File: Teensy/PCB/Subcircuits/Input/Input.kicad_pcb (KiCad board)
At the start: 2 copper layers, 4 parts

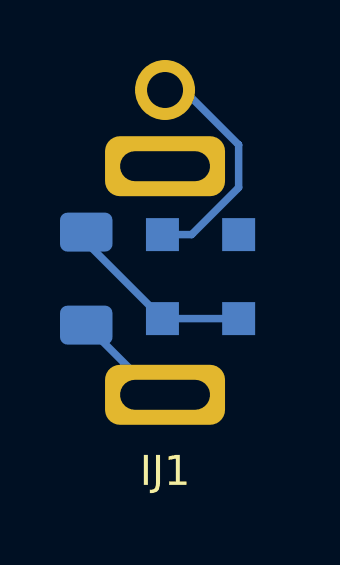
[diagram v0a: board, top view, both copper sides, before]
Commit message: Added Panel PCBs
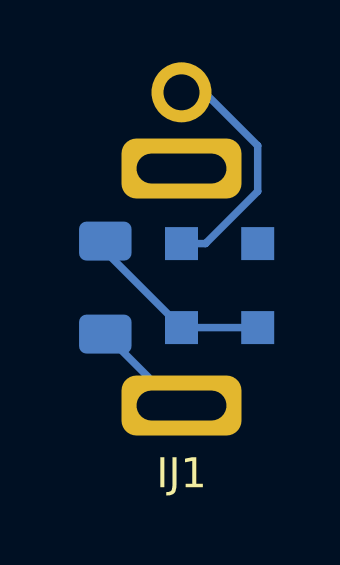
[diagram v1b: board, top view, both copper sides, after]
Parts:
- moved ID1 0.70 mm to (88.9, 90.3)
- moved IR1 0.70 mm to (86.4, 90.3)
- moved ID2 0.70 mm to (91.4, 90.3)
- moved IJ1 0.55 mm to (88.9, 88.9)
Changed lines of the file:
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@@
   (net 0 "")
   (footprint "Perfboard:3.5mm Jack Perfboard" (layer "F.Cu")
-    (at 88.351 88.822274)
-    (property "Sheetfile" "../Subcircuits/Input/Input.kicad_sch")
-    (property "Sheetname" "Attack_Time_Mod_In")
+    (at 88.9 88.9)
+    (property "Sheetfile" "Input.kicad_sch")
+    (property "Sheetname" "")
     (attr through_hole)
     (fp_text reference "IJ1" (at 0 7.62 unlocked) (layer "F.SilkS")
@@
       (effects (font (size 1 1) (thickness 0.15)))
     )
-    (fp_line (start 2.54 -3.81) (end 3.81 -3.81) (layer "Dwgs.User") (width 0.12))
-    (fp_line (start 2.54 -3.81) (end -2.54 -3.81) (layer "Dwgs.User") (width 0.12))
-    (fp_line (start -3.81 6.35) (end -2.54 6.35) (layer "Dwgs.User") (width 0.12))
-    (fp_line (start -2.54 6.35) (end 2.54 6.35) (layer "Dwgs.User") (width 0.12))
-    (fp_line (start 3.81 6.35) (end 2.54 6.35) (layer "Dwgs.User") (width 0.12))
-    (fp_line (start 3.81 -3.81) (end 3.81 6.35) (layer "Dwgs.User") (width 0.12))
-    (fp_line (start -3.81 -3.81) (end -3.81 6.35) (layer "Dwgs.User") (width 0.12))
-    (fp_line (start -2.54 -3.81) (end -3.81 -3.81) (layer "Dwgs.User") (width 0.12))
-    (fp_circle (center 0 0.83) (end 3.25 0.83) (layer "User.2") (width 0.12) (fill none))
+    (fp_rect (start -3.8 -3.94) (end 3.8 6.56) (layer "F.CrtYd") (width 0.12) (fill none))
+    (fp_circle (center 0 0.86) (end 3.25 0.86) (layer "User.2") (width 0.12) (fill none))
     (pad "G" thru_hole circle (at 0 -5.08) (size 2 2) (drill 1.2) (layers *.Cu *.Mask)
       (pintype "passive"))
     (pad "S" thru_hole roundrect (at 0 -2.54) (size 4 2) (drill oval 3 1) (layers *.Cu *.Mask) (roundrect_rratio 0.25)
       (pintype "passive"))
-    (pad "T" thru_hole roundrect (at 0 5.08) (size 4 2) (drill oval 3 1) (layers *.Cu *.Mask) (roundrect_rratio 0.25)
+    (pad "T" thru_hole roundrect (at 0 5.36) (size 4 2) (drill oval 3 1) (layers *.Cu *.Mask) (roundrect_rratio 0.25)
       (pintype "passive"))
     (model "C:/Users/Florian/Documents/KiCad/6.0/3dmodels/PTV09/PJ301M-12 Thonkiconn v0.2.stp"
-      (offset (xyz 0 -1 0))
+      (offset (xyz 0 -1.5 0))
       (scale (xyz 1 1 1))
       (rotate (xyz 0 0 180))
@@
   )
   (footprint "Diode_SMD:D_SOD-123F" (layer "B.Cu")
-    (at 90.805 89.962274 -90)
+    (at 91.44 90.261875 -90)
     (descr "D_SOD-123F")
     (tags "D_SOD-123F")
-    (property "Sheetfile" "../Subcircuits/Input/Input.kicad_sch")
-    (property "Sheetname" "Attack_Time_Mod_In")
+    (property "Sheetfile" "Input.kicad_sch")
+    (property "Sheetname" "")
     (attr smd)
-    (fp_text reference "ID2" (at -0.127 1.905 90) (layer "B.SilkS")
+    (fp_text reference "ID2" (at -0.127 1.905 90) (layer "B.SilkS") hide
       (effects (font (size 1 1) (thickness 0.15)) (justify mirror))
     )
-    (fp_text value "240mV" (at 0 -2.1 90) (layer "B.Fab")
+    (fp_text value "240mV" (at -0.046274 -2.159 90) (layer "B.SilkS")
       (effects (font (size 1 1) (thickness 0.15)) (justify mirror))
     )
@@
   )
   (footprint "Resistor_SMD:R_1206_3216Metric_Pad1.30x1.75mm_HandSolder" (layer "B.Cu")
-    (at 85.725 90.029274 90)
+    (at 86.36 90.328875 90)
     (descr "Resistor SMD 1206 (3216 Metric), square (rectangular) end terminal, IPC_7351 nominal with elongated pad for handsoldering. (Body size source: IPC-SM-782 page 72, https://www.pcb-3d.com/wordpress/wp-content/uploads/ipc-sm-782a_amendment_1_and_2.pdf), generated with kicad-footprint-generator")
     (tags "resistor handsolder")
-    (property "Sheetfile" "../Subcircuits/Input/Input.kicad_sch")
-    (property "Sheetname" "Attack_Time_Mod_In")
+    (property "Sheetfile" "Input.kicad_sch")
+    (property "Sheetname" "")
     (attr smd)
-    (fp_text reference "IR1" (at 0 1.82 90) (layer "B.SilkS")
+    (fp_text reference "IR1" (at 0 1.82 90) (layer "B.SilkS") hide
       (effects (font (size 1 1) (thickness 0.15)) (justify mirror))
     )
-    (fp_text value "1k" (at 0 -1.82 90) (layer "B.Fab")
+    (fp_text value "1k" (at 0.113274 -1.905 90) (layer "B.SilkS")
       (effects (font (size 1 1) (thickness 0.15)) (justify mirror))
     )
@@
   )
   (footprint "Diode_SMD:D_SOD-123F" (layer "B.Cu")
-    (at 88.265 89.962274 90)
+    (at 88.9 90.261875 90)
     (descr "D_SOD-123F")
     (tags "D_SOD-123F")
-    (property "Sheetfile" "../Subcircuits/Input/Input.kicad_sch")
-    (property "Sheetname" "Attack_Time_Mod_In")
+    (property "Sheetfile" "Input.kicad_sch")
+    (property "Sheetname" "")
     (attr smd)
-    (fp_text reference "ID1" (at -0.127 1.905 90) (layer "B.SilkS")
+    (fp_text reference "ID1" (at -0.127 1.905 90) (layer "B.SilkS") hide
       (effects (font (size 1 1) (thickness 0.15)) (justify mirror))
     )
@@
     )
   )
-  (segment (start 88.351 93.902274) (end 88.048 93.902274) (width 0.25) (layer "F.Cu") (net 0))
-  (segment (start 90.805 86.995) (end 90.805 85.569548) (width 0.25) (layer "B.Cu") (net 0))
-  (segment (start 85.725 88.479274) (end 85.725 88.822274) (width 0.25) (layer "B.Cu") (net 0))
-  (segment (start 88.265 91.362274) (end 90.805 91.362274) (width 0.25) (layer "B.Cu") (net 0))
-  (segment (start 88.265 88.562274) (end 89.237726 88.562274) (width 0.25) (layer "B.Cu") (net 0))
-  (segment (start 88.977726 83.742274) (end 88.351 83.742274) (width 0.25) (layer "B.Cu") (net 0))
-  (segment (start 88.048 93.902274) (end 85.725 91.579274) (width 0.25) (layer "B.Cu") (net 0))
-  (segment (start 90.805 85.569548) (end 88.977726 83.742274) (width 0.25) (layer "B.Cu") (net 0))
-  (segment (start 89.237726 88.562274) (end 90.805 86.995) (width 0.25) (layer "B.Cu") (net 0))
-  (segment (start 85.725 88.822274) (end 88.265 91.362274) (width 0.25) (layer "B.Cu") (net 0))
-  (segment (start 88.351 93.902274) (end 88.048 93.902274) (width 0.25) (layer "B.Cu") (net 0))
+  (segment (start 91.44 87.121875) (end 91.44 85.598) (width 0.25) (layer "B.Cu") (net 0))
+  (segment (start 86.36 88.778875) (end 86.36 89.121875) (width 0.25) (layer "B.Cu") (net 0))
+  (segment (start 88.9 91.661875) (end 91.44 91.661875) (width 0.25) (layer "B.Cu") (net 0))
+  (segment (start 88.741125 94.26) (end 88.9 94.26) (width 0.25) (layer "B.Cu") (net 0))
+  (segment (start 89.662 83.82) (end 88.9 83.82) (width 0.25) (layer "B.Cu") (net 0))
+  (segment (start 91.44 85.598) (end 89.662 83.82) (width 0.25) (layer "B.Cu") (net 0))
+  (segment (start 86.36 91.878875) (end 88.741125 94.26) (width 0.25) (layer "B.Cu") (net 0))
+  (segment (start 86.36 89.121875) (end 88.9 91.661875) (width 0.25) (layer "B.Cu") (net 0))
+  (segment (start 89.7 88.861875) (end 91.44 87.121875) (width 0.25) (layer "B.Cu") (net 0))
+  (segment (start 88.9 88.861875) (end 89.7 88.861875) (width 0.25) (layer "B.Cu") (net 0))
 )

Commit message: Made NPTH holes 0.5mm bigger; adjusted diode pads for better solderability
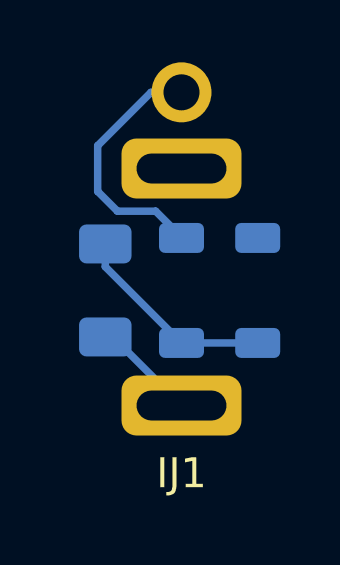
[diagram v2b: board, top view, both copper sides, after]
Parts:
- ID1, ID2: footprint Diode_SMD:D_SOD-123F -> Misc:D_SOD-123 Handsolder
- moved ID1 0.16 mm to (88.9, 90.4)
- moved ID2 0.16 mm to (91.4, 90.4)
- moved IR1 0.10 mm to (86.4, 90.4)
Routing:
- net (no net): track 18.1 -> 18.9 mm
